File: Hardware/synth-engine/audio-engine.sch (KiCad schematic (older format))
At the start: 1 part

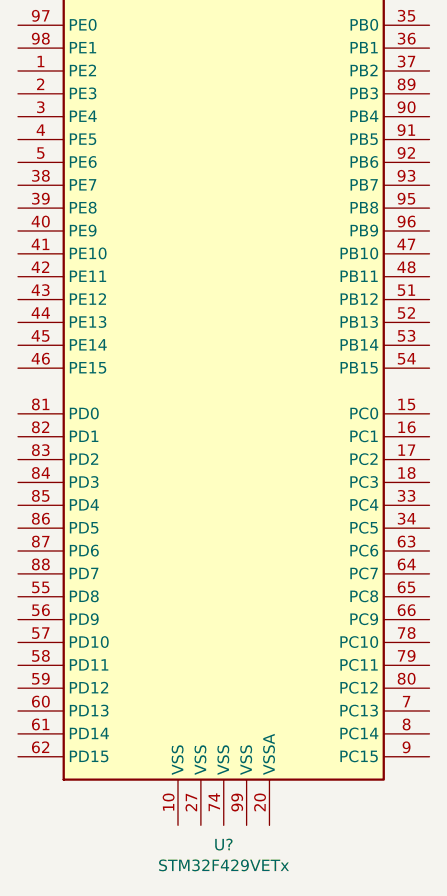
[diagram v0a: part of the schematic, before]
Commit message: fix some ground/VREF mixups on filter schematic
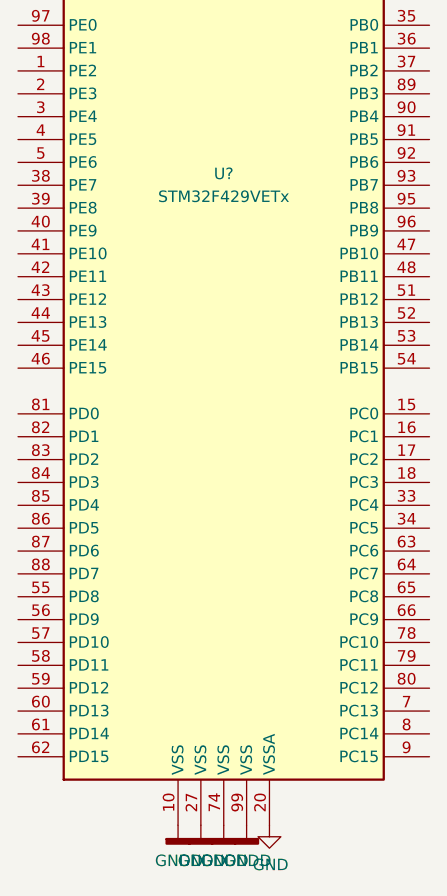
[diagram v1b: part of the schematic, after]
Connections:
- net GNDD: now reaches U?.10 (VSS)
- net GNDD: now also U?.27 (VSS), U?.74 (VSS), U?.99 (VSS)
- net GND: now reaches U?.20 (VSSA)
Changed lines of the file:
@@
 U 1 1 5DDC7DCC
 P 3700 4000
-F 0 "U?" H 3700 1114 50  0000 C CNN
-F 1 "STM32F429VETx" H 3700 1023 50  0000 C CNN
+F 0 "U?" H 3700 4050 50  0000 C CNN
+F 1 "STM32F429VETx" H 3700 3950 50  0000 C CNN
 F 2 "Package_QFP:LQFP-100_14x14mm_P0.5mm" H 3000 1400 50  0001 R CNN
 F 3 "http://www.st.com/st-web-ui/static/active/en/resource/technical/document/datasheet/DM00071990.pdf" H 3700 4000 50  0001 C CNN
@@
 	1    0    0    -1
 $EndComp
+$Comp
+L power:GNDD #PWR?
+U 1 1 5DD6DEB7
+P 3500 6800
+F 0 "#PWR?" H 3500 6550 50  0001 C CNN
+F 1 "GNDD" H 3504 6645 50  0000 C CNN
+F 2 "" H 3500 6800 50  0001 C CNN
+F 3 "" H 3500 6800 50  0001 C CNN
+	1    3500 6800
+	1    0    0    -1
+$EndComp
+$Comp
+L power:GNDD #PWR?
+U 1 1 5DD6DECB
+P 3600 6800
+F 0 "#PWR?" H 3600 6550 50  0001 C CNN
+F 1 "GNDD" H 3604 6645 50  0000 C CNN
+F 2 "" H 3600 6800 50  0001 C CNN
+F 3 "" H 3600 6800 50  0001 C CNN
+	1    3600 6800
+	1    0    0    -1
+$EndComp
+$Comp
+L power:GNDD #PWR?
+U 1 1 5DD6DED8
+P 3700 6800
+F 0 "#PWR?" H 3700 6550 50  0001 C CNN
+F 1 "GNDD" H 3704 6645 50  0000 C CNN
+F 2 "" H 3700 6800 50  0001 C CNN
+F 3 "" H 3700 6800 50  0001 C CNN
+	1    3700 6800
+	1    0    0    -1
+$EndComp
+$Comp
+L power:GNDD #PWR?
+U 1 1 5DD6DEE5
+P 3800 6800
+F 0 "#PWR?" H 3800 6550 50  0001 C CNN
+F 1 "GNDD" H 3804 6645 50  0000 C CNN
+F 2 "" H 3800 6800 50  0001 C CNN
+F 3 "" H 3800 6800 50  0001 C CNN
+	1    3800 6800
+	1    0    0    -1
+$EndComp
+$Comp
+L power:GND #PWR?
+U 1 1 5DD6DF42
+P 3900 6800
+F 0 "#PWR?" H 3900 6550 50  0001 C CNN
+F 1 "GND" H 3905 6627 50  0000 C CNN
+F 2 "" H 3900 6800 50  0001 C CNN
+F 3 "" H 3900 6800 50  0001 C CNN
+	1    3900 6800
+	1    0    0    -1
+$EndComp

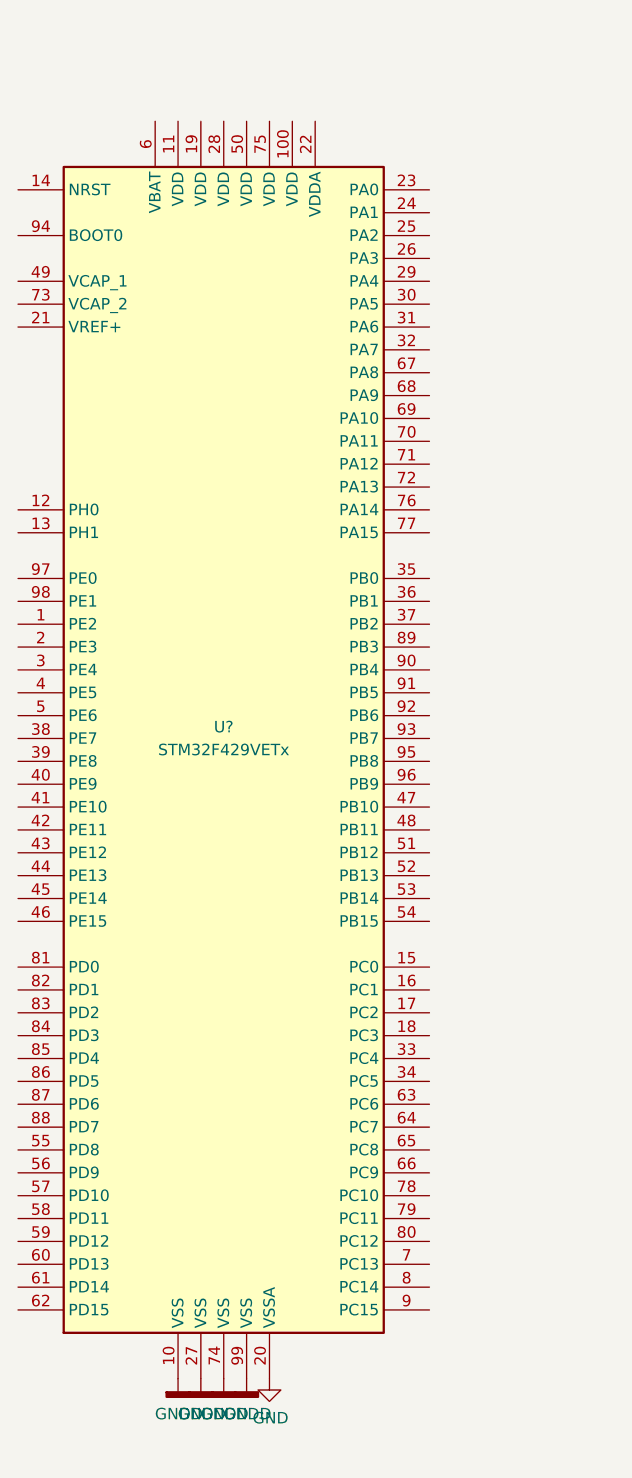
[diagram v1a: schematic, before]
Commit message: add STM32 voltage rails and bypass capacitors
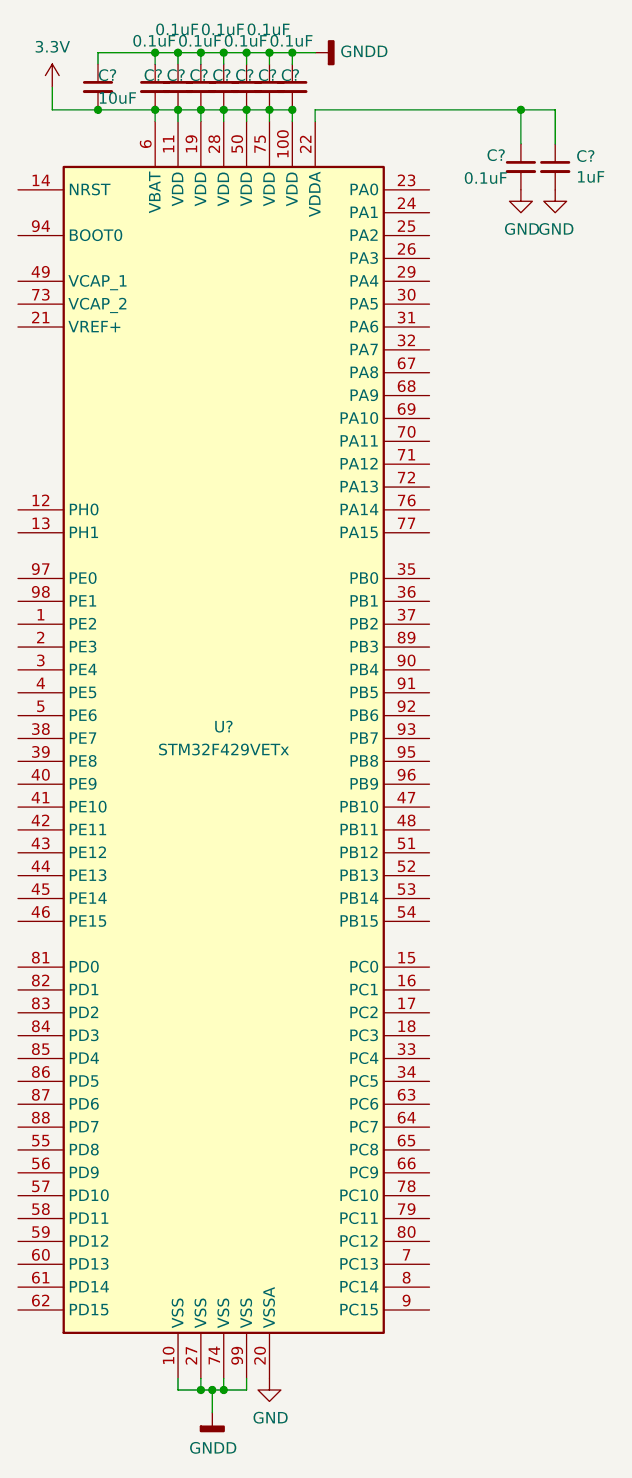
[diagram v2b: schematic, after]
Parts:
- added C? (x8): 0.1uF, symbol Device:C_Small
- added C?: 1uF, symbol Device:C_Small
- added C?: 10uF, symbol Device:C_Small
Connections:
- net GND: now also C?.2, C?.2
- net GNDD: now also C?.1, C?.1, C?.1, C?.1, C?.1, C?.1, C?.1, C?.1
- net 3.3V: now reaches U?.100 (VDD)
- net 3.3V: now also U?.11 (VDD), U?.19 (VDD), U?.28 (VDD), U?.50 (VDD), U?.6 (VBAT), U?.75 (VDD), C?.2, C?.2, C?.2, C?.2, C?.2, C?.2, C?.2, C?.2
- net at U?.22 (VDDA): now also C?.1, C?.1

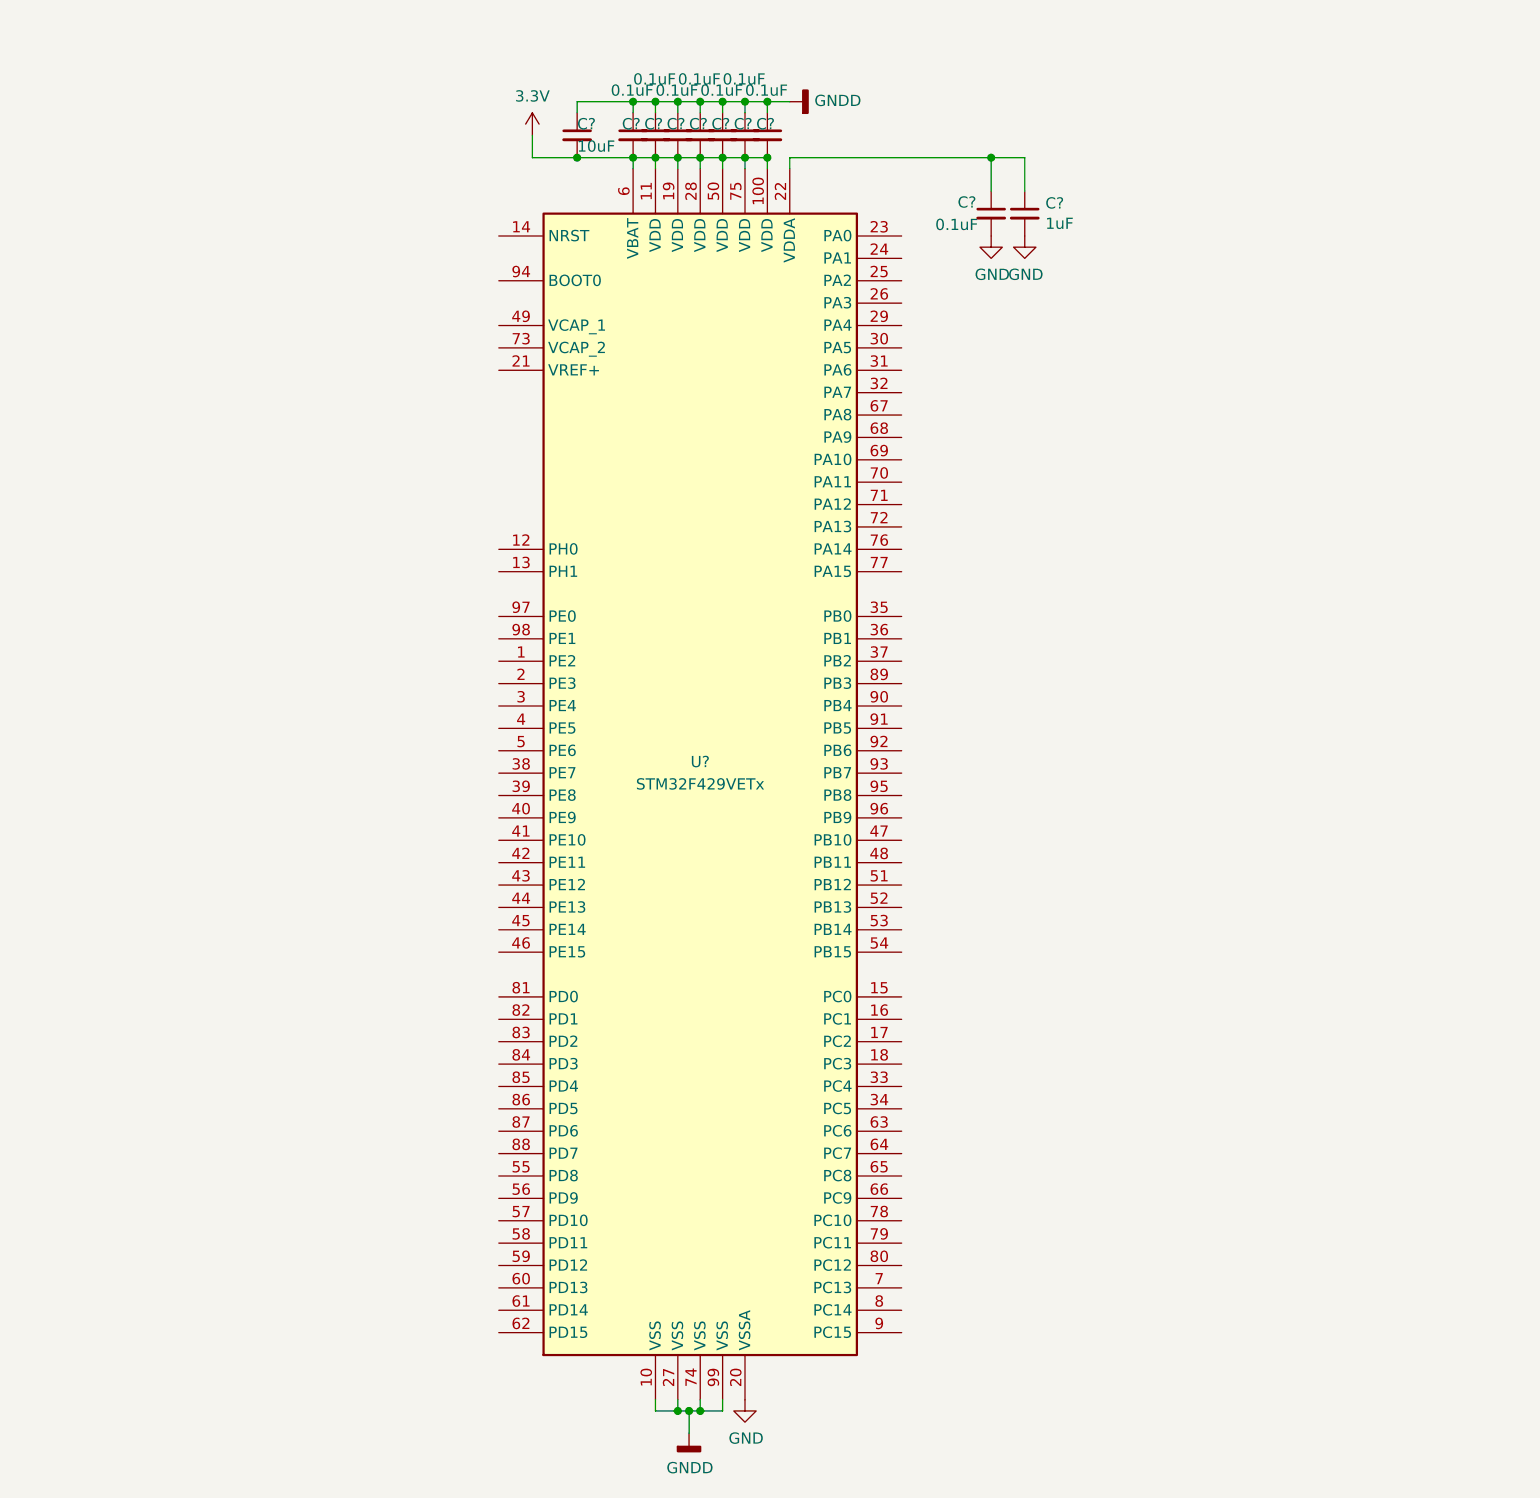
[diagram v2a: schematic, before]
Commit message: add SWD debugging/programming header to STM32 schematic
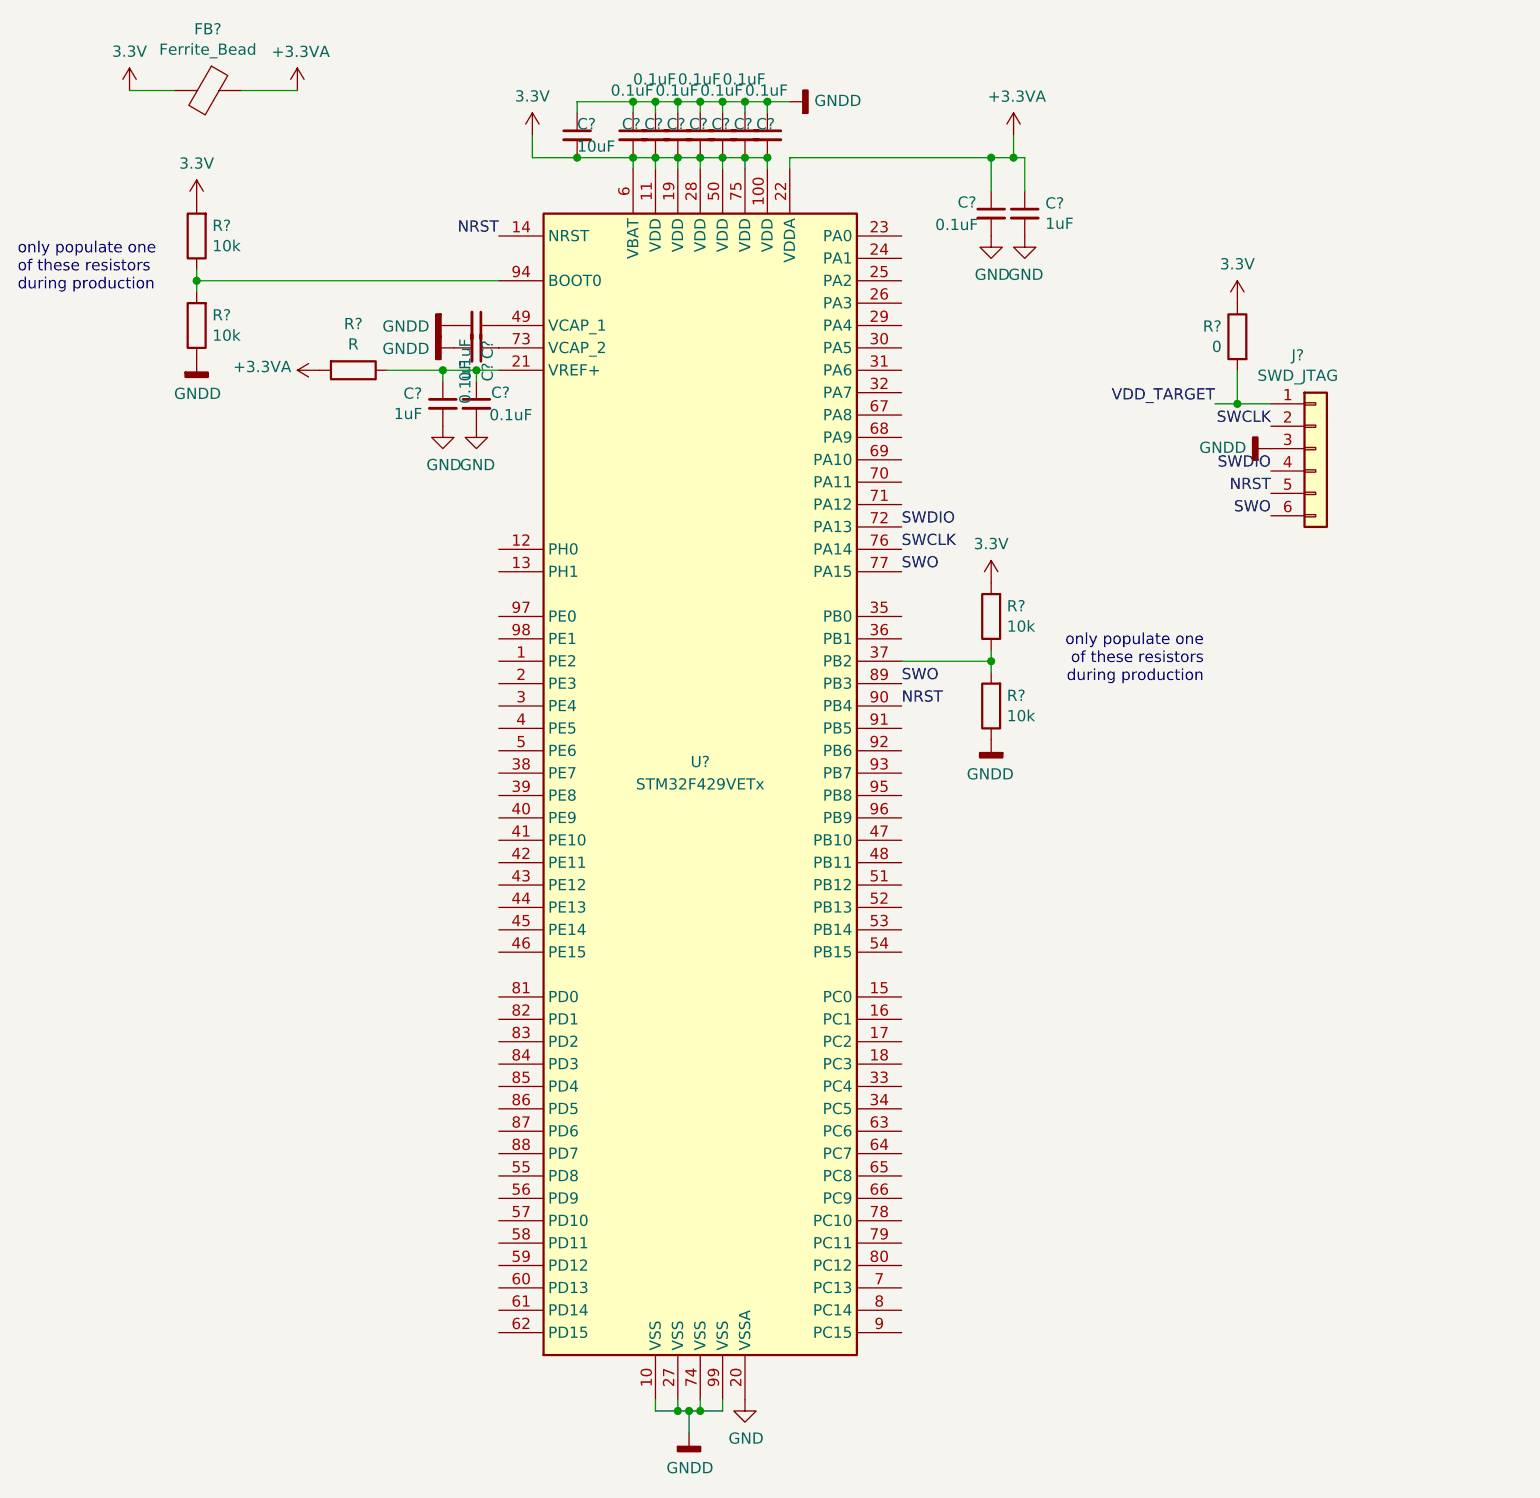
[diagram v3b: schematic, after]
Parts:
- added C? (x3): 0.1uF, symbol Device:C_Small
- added C?: 1uF, symbol Device:C_Small
- added FB?: Ferrite_Bead, symbol Device:Ferrite_Bead
- added J?: SWD_JTAG, symbol Connector_Generic:Conn_01x06
- added R?: R, symbol Device:R
- added R? (x4): 10k, symbol Device:R
- added R?: 0, symbol Device:R
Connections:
- net 3.3V: now also FB?.2, R?.1, R?.2, R?.2
- net GND: now also C?.2, C?.2
- net GNDD: now also C?.2, C?.2, J?.3 (Pin_3), R?.1, R?.1
- net +3.3VA: now reaches C?.1, C?.1, U?.22 (VDDA)
- net +3.3VA: now also FB?.1, R?.2
- net NRST: now reaches U?.14 (NRST)
- net NRST: now also U?.90 (PB4), J?.5 (Pin_5)
- net at U?.21 (VREF+): now also C?.1, C?.1, R?.1
- net at U?.37 (PB2): now also R?.1, R?.2
- net at U?.49 (VCAP_1): now also C?.1
- net SWDIO: now reaches U?.72 (PA13)
- net SWDIO: now also J?.4 (Pin_4)
- net at U?.73 (VCAP_2): now also C?.1
- net SWCLK: now reaches U?.76 (PA14)
- net SWCLK: now also J?.2 (Pin_2)
- net SWO: now reaches U?.77 (PA15)
- net SWO: now also U?.89 (PB3), J?.6 (Pin_6)
- net at U?.94 (BOOT0): now also R?.1, R?.2
- new net VDD_TARGET: J?.1 (Pin_1), R?.2
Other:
- note added: "only populate one\nof these resistors\nduring production"
